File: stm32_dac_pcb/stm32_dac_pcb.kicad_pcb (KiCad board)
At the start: 2 copper layers, 63.1 x 21.8 mm, 52 parts, among them J1 Conn_01x03, J2 Conn_01x05, J3 USB_C_Receptacle_USB2.0, J4 AudioJack4, SW1 SW_Push, SW2 SW_Push, U1 AP1117-33, U2 AP1117-33, U3 STM32F411CEUx, U4 PCM5102A, Y1 25MHz, 9pF

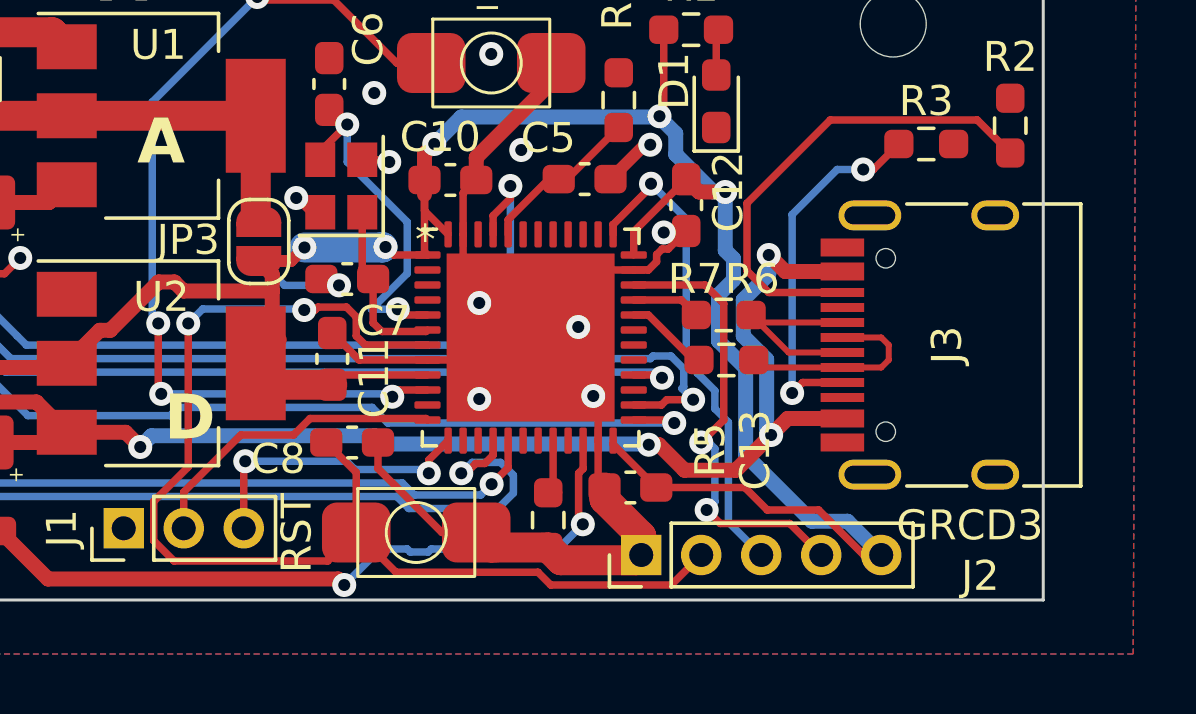
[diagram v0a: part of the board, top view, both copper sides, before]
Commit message: Convert to SOICbite SWD+UART connector for Rev 3
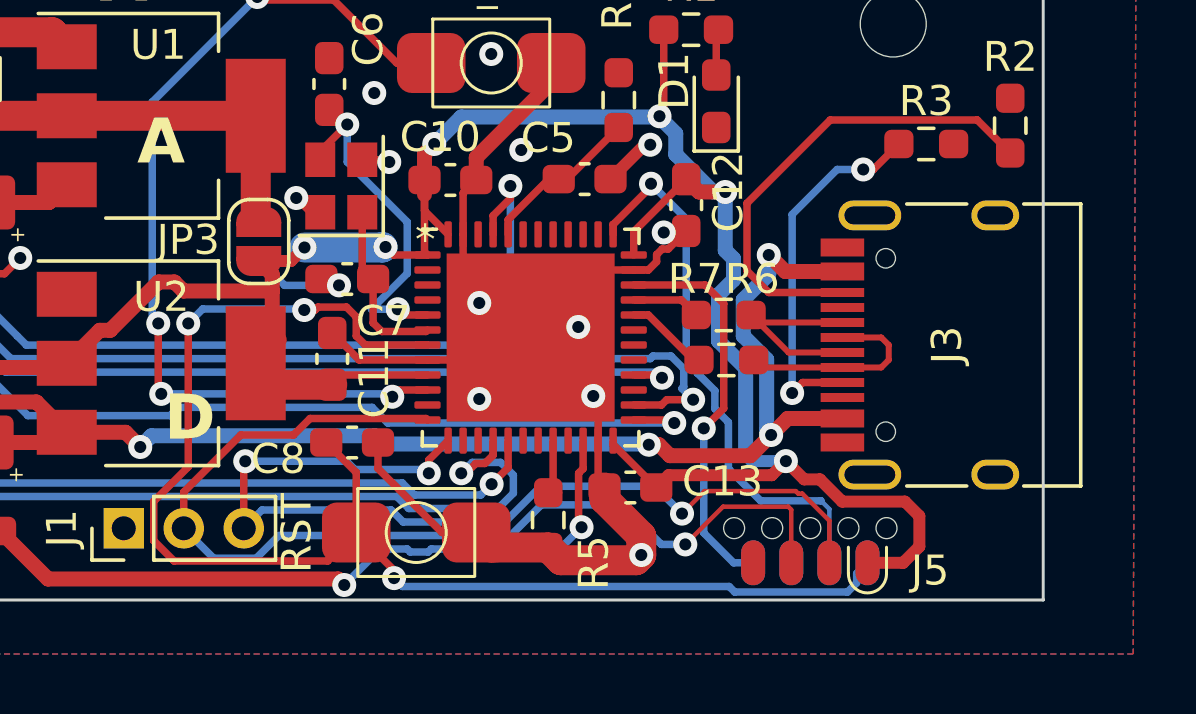
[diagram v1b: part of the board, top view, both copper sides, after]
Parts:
- removed J2: Conn_01x05, Connector_PinHeader_2.00mm:PinHeader_1x05_P2.00mm_Vertical
- added J5: Conn_01x08, 0_project_fp_lib:SOIC_clipProgSmall, F.Cu at (151.1, 106.5)
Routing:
- net /microcontroller_sheet/UART_TX_MISO: track 10.4 -> 34.6 mm, vias 0 -> 1
- net /microcontroller_sheet/UART_RX_MOSI: track 9.89 -> 32.8 mm, vias 2 -> 3
- net /microcontroller_sheet/NRST: track 40.3 -> 46.3 mm, vias 2 -> 3
- net /microcontroller_sheet/SWCLK: track 16.1 -> 18.5 mm
- net /microcontroller_sheet/SWDIO: track 15.3 -> 13.5 mm, vias 2 -> 1
- net +3.3V: track 100.9 -> 100.8 mm, vias 7 -> 8
- net GND: vias 18 -> 19
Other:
- board text added: "Rev 3 2024-11-xx STM32 DAC DeflateAwning"
- board text removed: "GRCD3"
- board text removed: "Rev 2 2024-10-22 STM32 DAC DeflateAwning"
